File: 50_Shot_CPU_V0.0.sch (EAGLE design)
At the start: 74 parts, among them IC1 PIC24FJ128GA010, J1 J12, J10 22-23-2021, J11 22-23-2061, J12 A311422_nd, J13 22-23-2021, J14 22-23-2021, J2 J2, J3 22-23-2021, J4 22-23-2021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

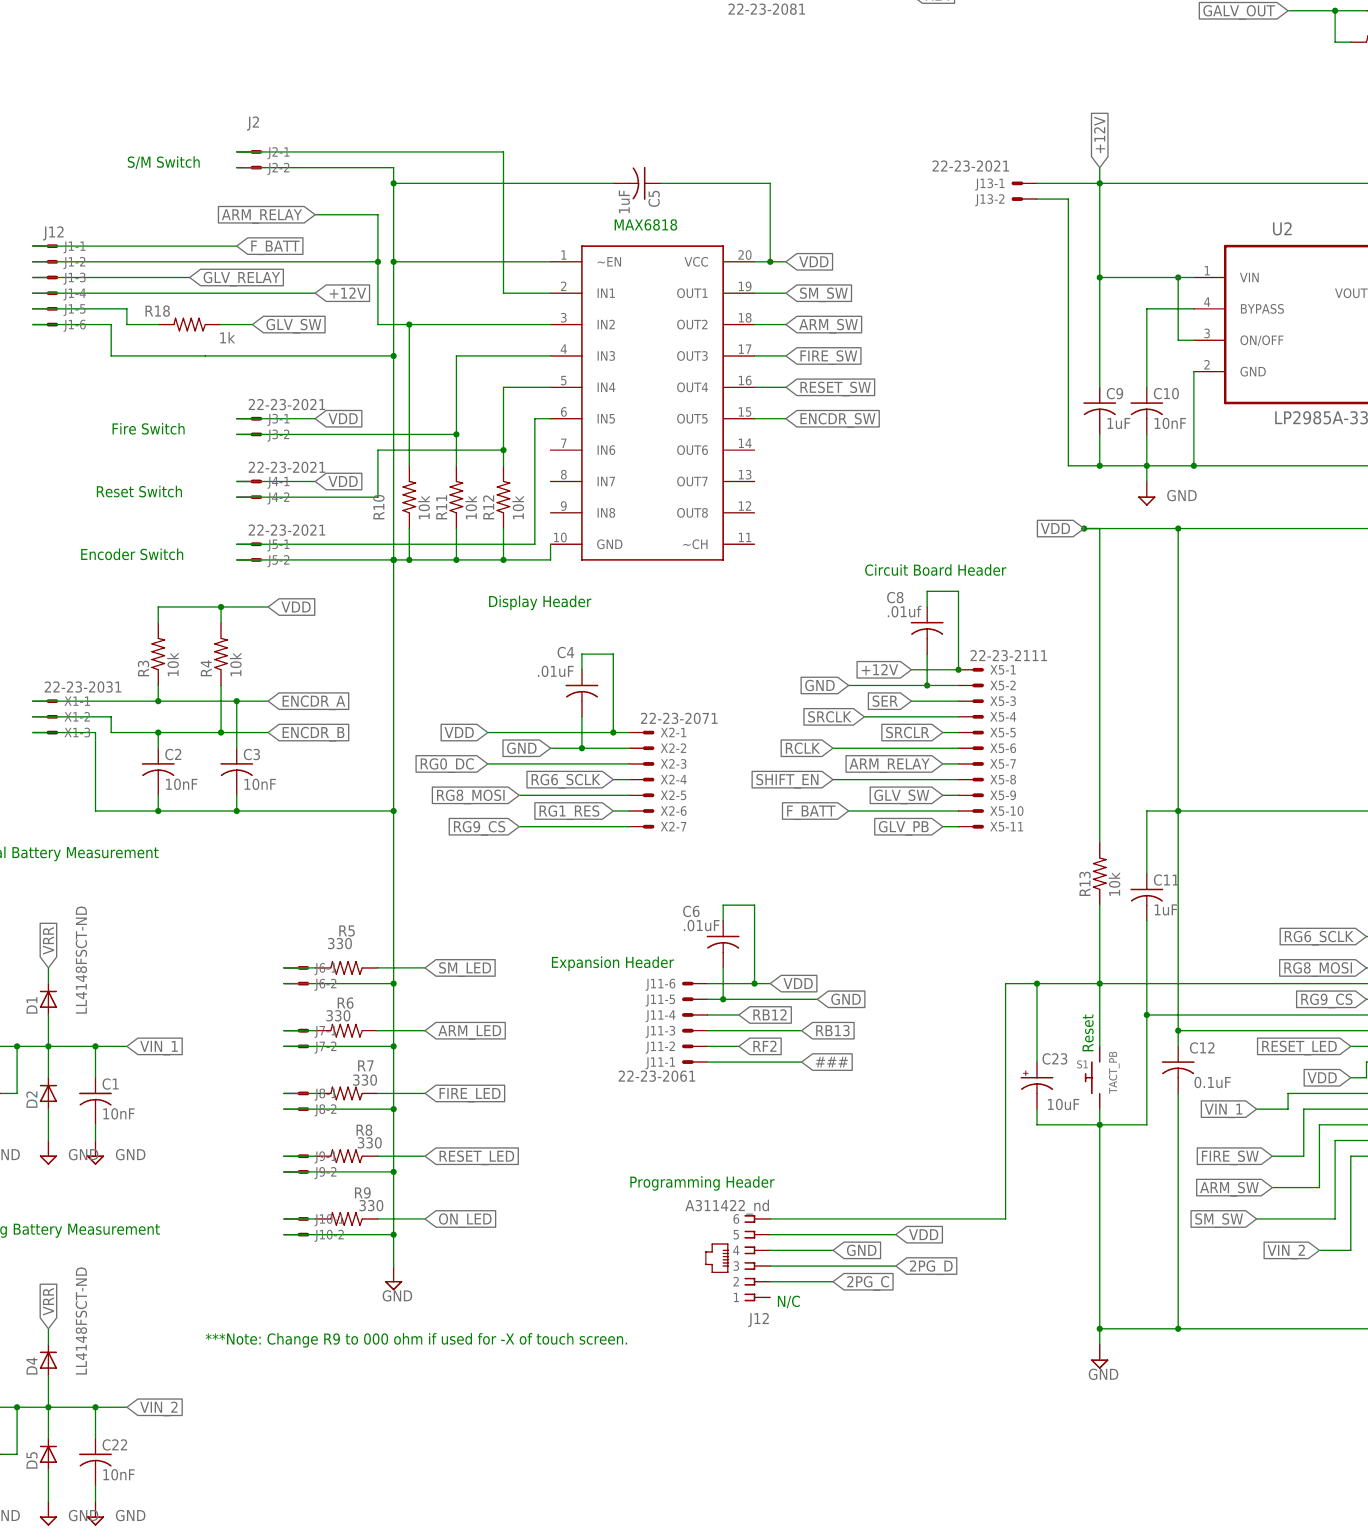
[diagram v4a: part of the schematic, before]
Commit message: removed SM switch (RB2)
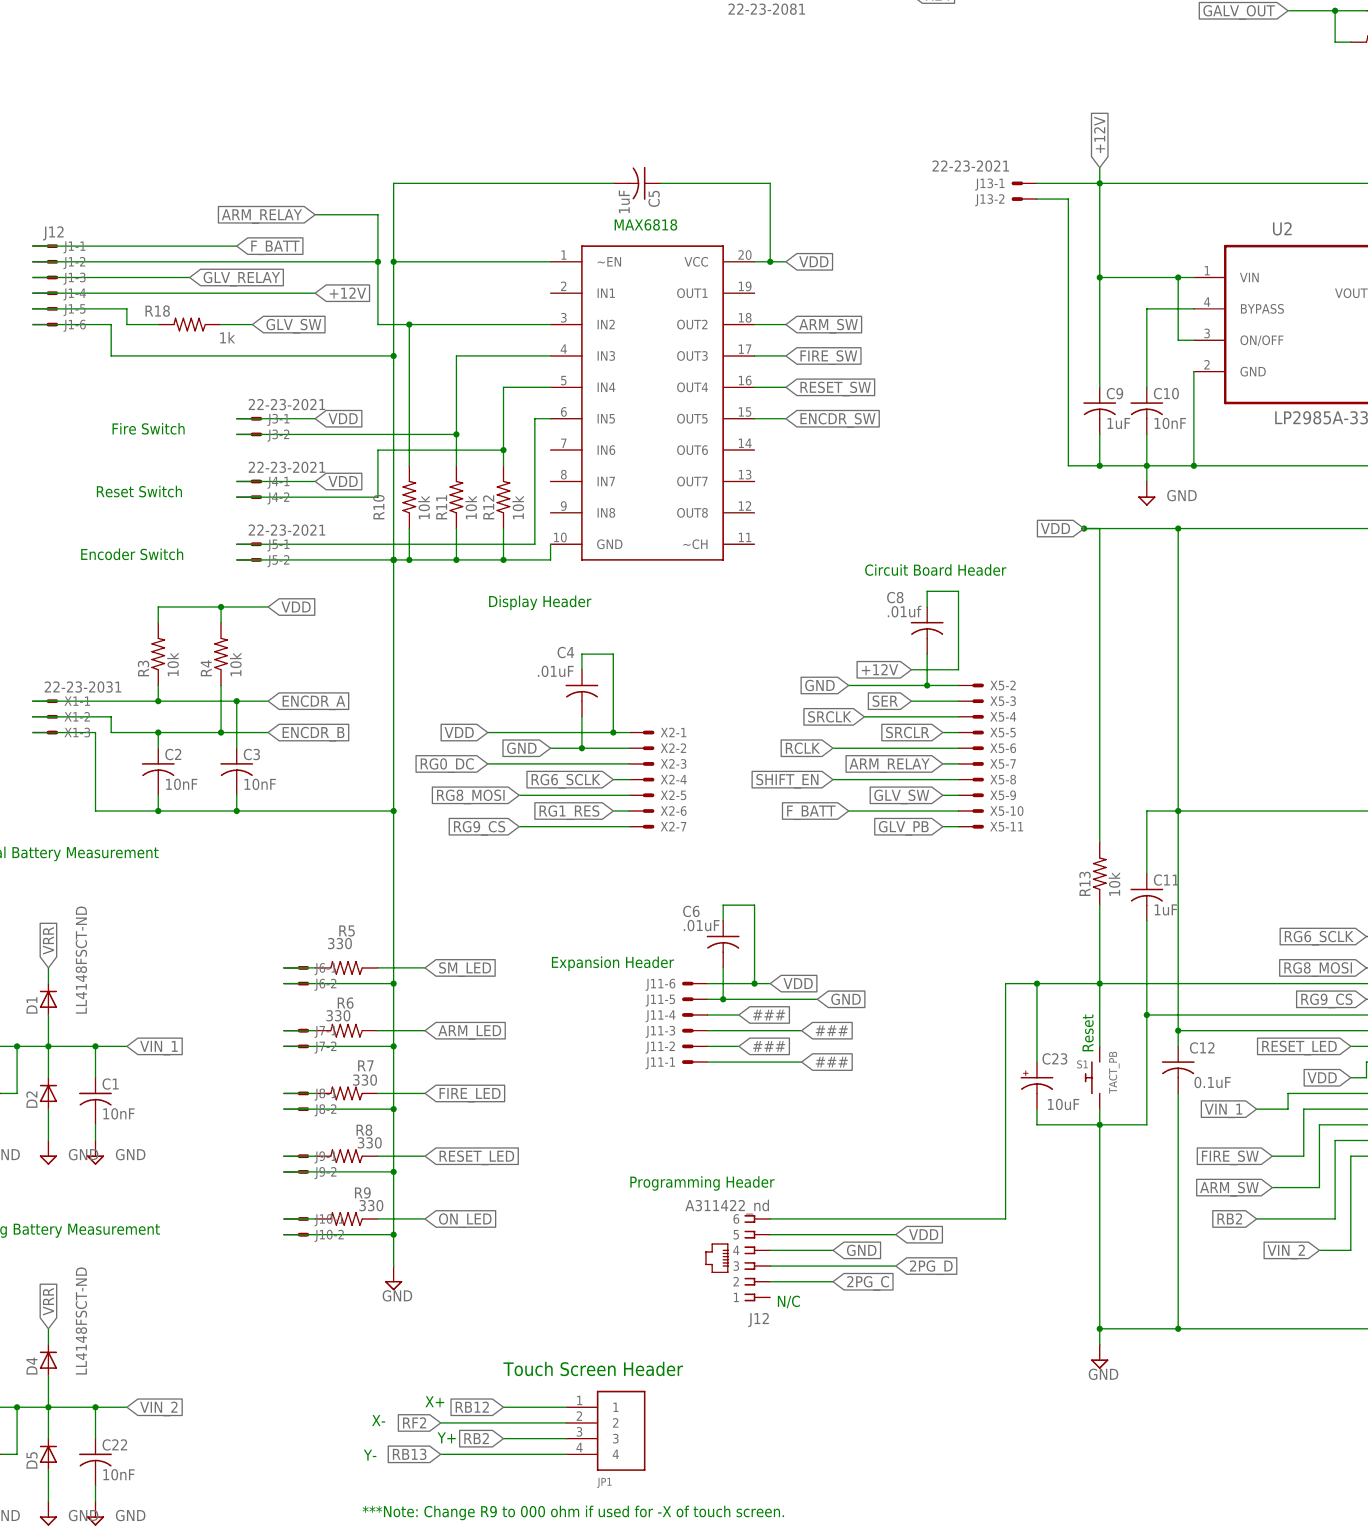
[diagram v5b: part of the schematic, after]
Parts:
- removed J2: J2, Mine:22-23-2021
- added JP1: SHERLOCK_4PIN_RGT, Mine:SHERLOCK_4PIN_RGT
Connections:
- removed net N$2: J2-1.S, U1.IN1
- removed net SM_SW: IC1.C2IN-/AN2/SS1/CN4/RB2, U1.OUT1
- new net RB2: IC1.C2IN-/AN2/SS1/CN4/RB2, JP1.3
- net ###: now also J11-2.S, J11-3.S, J11-4.S
- net +12V: no longer X5-1.S
- net GND: no longer J2-2.S
- net RB12: now also JP1.1; no longer J11-4.S
- net RB13: now also JP1.4; no longer J11-3.S
- net RF2: now also JP1.2; no longer J11-2.S
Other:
- note added: "Touch Screen Header"
- note added: "X+"
- note added: "X-"
- note added: "Y+"
- note added: "Y-"
- note removed: "S/M Switch"

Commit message: converted SPI display header
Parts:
- removed X2: 22-23-2071, con-molex:22-23-2071
- added JP2: SHERLOCK_8PIN_RGT, Mine:SHERLOCK_8PIN_RGT
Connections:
- net RB12 renamed RB12_X+
- net RB13 renamed RB13_Y-
- net RB2 renamed RB2_Y+
- net RF2 renamed RF2_X-
- new net RG7_MISO: IC1.PMA4/SDI2/CN9/RG7, JP2.8
- net +12V: now also C4.1, JP2.1
- net GND: now also JP2.2; no longer X2-2.S
- net RG0_DC: now also JP2.3; no longer X2-3.S
- net RG1_RES: now also JP2.6; no longer X2-6.S
- net RG6_SCLK: now also JP2.4; no longer X2-4.S
- net RG8_MOSI: now also JP2.5; no longer X2-5.S
- net RG9_CS: now also JP2.7; no longer X2-7.S
- net VDD: no longer C4.1, X2-1.S
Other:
- note added: "SPI Display Header"
- note removed: "Display Header"
- note removed: "X+"
- note removed: "X-"
- note removed: "Y+"
- note removed: "Y-"

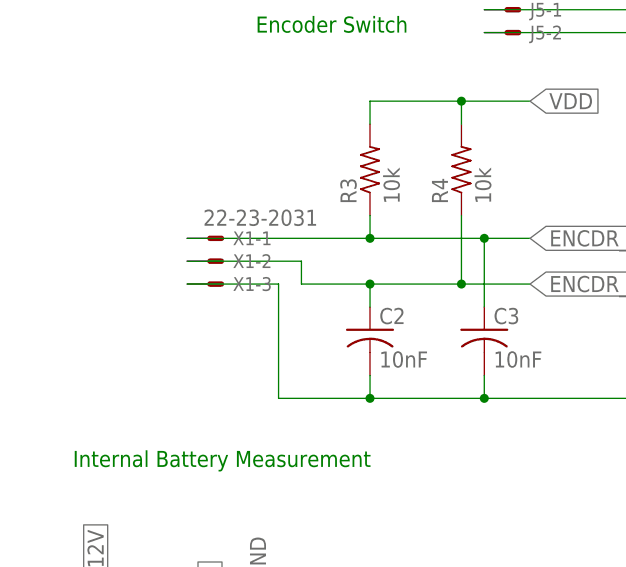
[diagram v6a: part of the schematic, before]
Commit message: converted rotary encoder header
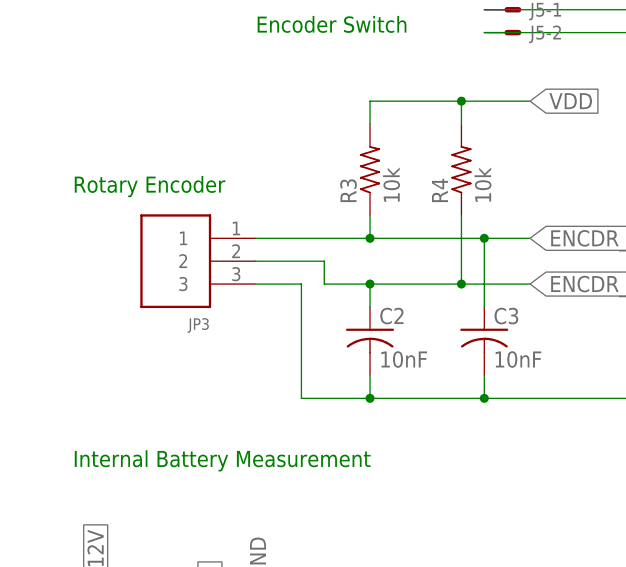
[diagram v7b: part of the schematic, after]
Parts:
- removed X1: 22-23-2031, Mine:22-23-2031
- added JP3: SHERLOCK_3PIN_RGT, Mine:SHERLOCK_3PIN_RGT
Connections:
- net ENCDR_A: now also JP3.1; no longer X1-1.S
- net ENCDR_B: now also JP3.2; no longer X1-2.S
- net GND: now also JP3.3; no longer X1-3.S
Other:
- note added: "Rotary Encoder"
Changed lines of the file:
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@@
 <part name="C2" library="rcl" deviceset="C-US" device="C0805" value="10nF"/>
 <part name="C3" library="rcl" deviceset="C-US" device="C0805" value="10nF"/>
-<part name="X1" library="Mine" deviceset="22-23-2031" device=""/>
 <part name="C8" library="rcl" deviceset="C-US" device="C0805" value=".01uf"/>
 <part name="C4" library="rcl" deviceset="C-US" device="C0805" value=".01uF"/>
@@
 <part name="JP1" library="Mine" deviceset="SHERLOCK_4PIN_RGT" device=""/>
 <part name="JP2" library="Mine" deviceset="SHERLOCK_8PIN_RGT" device=""/>
+<part name="JP3" library="Mine" deviceset="SHERLOCK_3PIN_RGT" device=""/>
 </parts>
 <sheets>
@@
 <text x="144.78" y="162.56" size="1.778" layer="91">it worked, try yhis again</text>
 <text x="-81.28" y="-43.18" size="2.1844" layer="91">Touch Screen Header</text>
+<text x="-170.18" y="71.12" size="1.778" layer="91">Rotary Encoder</text>
 </plain>
 <instances>
@@
 <attribute name="VALUE" x="-123.444" y="51.689" size="1.778" layer="96"/>
 </instance>
-<instance part="X1" gate="-1" x="-154.94" y="66.04"/>
-<instance part="X1" gate="-2" x="-154.94" y="63.5"/>
-<instance part="X1" gate="-3" x="-154.94" y="60.96"/>
 <instance part="C8" gate="G$1" x="-12.7" y="78.74" smashed="yes">
 <attribute name="NAME" x="-19.304" y="81.915" size="1.778" layer="95"/>
@@
 <instance part="JP1" gate="G$1" x="-66.04" y="-50.8"/>
 <instance part="JP2" gate="G$1" x="-53.34" y="50.8"/>
+<instance part="JP3" gate="G$1" x="-154.94" y="63.5" rot="MR0"/>
 </instances>
 <busses>
@@
 <wire x1="-124.46" y1="50.8" x2="-124.46" y2="48.26" width="0.1524" layer="91"/>
 <junction x="-124.46" y="48.26"/>
-<pinref part="X1" gate="-3" pin="S"/>
-<wire x1="-157.48" y1="60.96" x2="-147.32" y2="60.96" width="0.1524" layer="91"/>
-<wire x1="-147.32" y1="60.96" x2="-147.32" y2="48.26" width="0.1524" layer="91"/>
-<wire x1="-147.32" y1="48.26" x2="-137.16" y2="48.26" width="0.1524" layer="91"/>
+<wire x1="-149.86" y1="60.96" x2="-144.78" y2="60.96" width="0.1524" layer="91"/>
+<wire x1="-144.78" y1="60.96" x2="-144.78" y2="48.26" width="0.1524" layer="91"/>
+<wire x1="-144.78" y1="48.26" x2="-137.16" y2="48.26" width="0.1524" layer="91"/>
 <junction x="-137.16" y="48.26"/>
+<pinref part="JP3" gate="G$1" pin="3"/>
 </segment>
 <segment>
@@
 <wire x1="-137.16" y1="66.04" x2="-124.46" y2="66.04" width="0.1524" layer="91"/>
 <label x="-119.38" y="66.04" size="1.778" layer="95" xref="yes"/>
-<pinref part="X1" gate="-1" pin="S"/>
 <wire x1="-124.46" y1="66.04" x2="-119.38" y2="66.04" width="0.1524" layer="91"/>
-<wire x1="-157.48" y1="66.04" x2="-137.16" y2="66.04" width="0.1524" layer="91"/>
+<wire x1="-149.86" y1="66.04" x2="-137.16" y2="66.04" width="0.1524" layer="91"/>
 <junction x="-137.16" y="66.04"/>
 <pinref part="C3" gate="G$1" pin="1"/>
 <wire x1="-124.46" y1="58.42" x2="-124.46" y2="66.04" width="0.1524" layer="91"/>
 <junction x="-124.46" y="66.04"/>
+<pinref part="JP3" gate="G$1" pin="1"/>
 </segment>
 </net>
@@
 <label x="-119.38" y="60.96" size="1.778" layer="95" xref="yes"/>
 <wire x1="-127" y1="60.96" x2="-119.38" y2="60.96" width="0.1524" layer="91"/>
-<pinref part="X1" gate="-2" pin="S"/>
-<wire x1="-157.48" y1="63.5" x2="-144.78" y2="63.5" width="0.1524" layer="91"/>
-<wire x1="-144.78" y1="63.5" x2="-144.78" y2="60.96" width="0.1524" layer="91"/>
-<wire x1="-144.78" y1="60.96" x2="-137.16" y2="60.96" width="0.1524" layer="91"/>
+<wire x1="-149.86" y1="63.5" x2="-142.24" y2="63.5" width="0.1524" layer="91"/>
+<wire x1="-142.24" y1="63.5" x2="-142.24" y2="60.96" width="0.1524" layer="91"/>
+<wire x1="-142.24" y1="60.96" x2="-137.16" y2="60.96" width="0.1524" layer="91"/>
 <junction x="-137.16" y="60.96"/>
 <pinref part="R4" gate="G$1" pin="1"/>
 <wire x1="-127" y1="68.58" x2="-127" y2="60.96" width="0.1524" layer="91"/>
 <junction x="-127" y="60.96"/>
-</segment>
-</net>
+<pinref part="JP3" gate="G$1" pin="2"/>
+</segment>
+</net>
